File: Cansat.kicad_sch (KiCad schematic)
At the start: 42 parts, among them J1 XT30_BATTERY, J10 Micro_SD_Card, J11 MAX17048_PLACEHOLDER, J2 BMP585_PLACEHOLDER, J3 BNO085_PLACEHOLDER, J4 CC1101_MODULE, J5 BUZZ_CONN, J6 SERVO_OUTPUT, J7 5V_BEC, J8 ESC_4IN1, J9 SGP41_PLACEHOLDER, SW1 SW_SPST, U1 XBee_SMT, U2 ESP32-S3-WROOM-1, U3 INA260, U4 GNSS_MODULE, U5 SHT4x

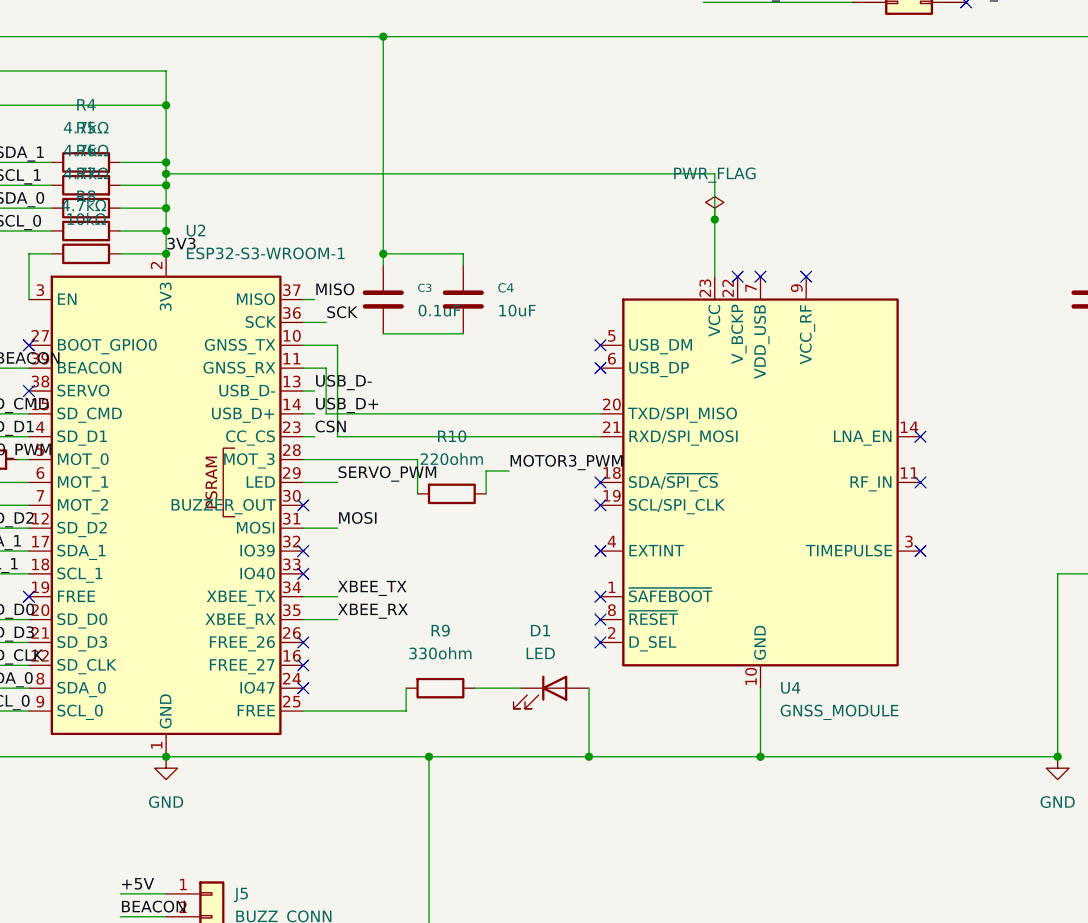
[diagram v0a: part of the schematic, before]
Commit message: replaced GNSS with NavIC 1x06 header
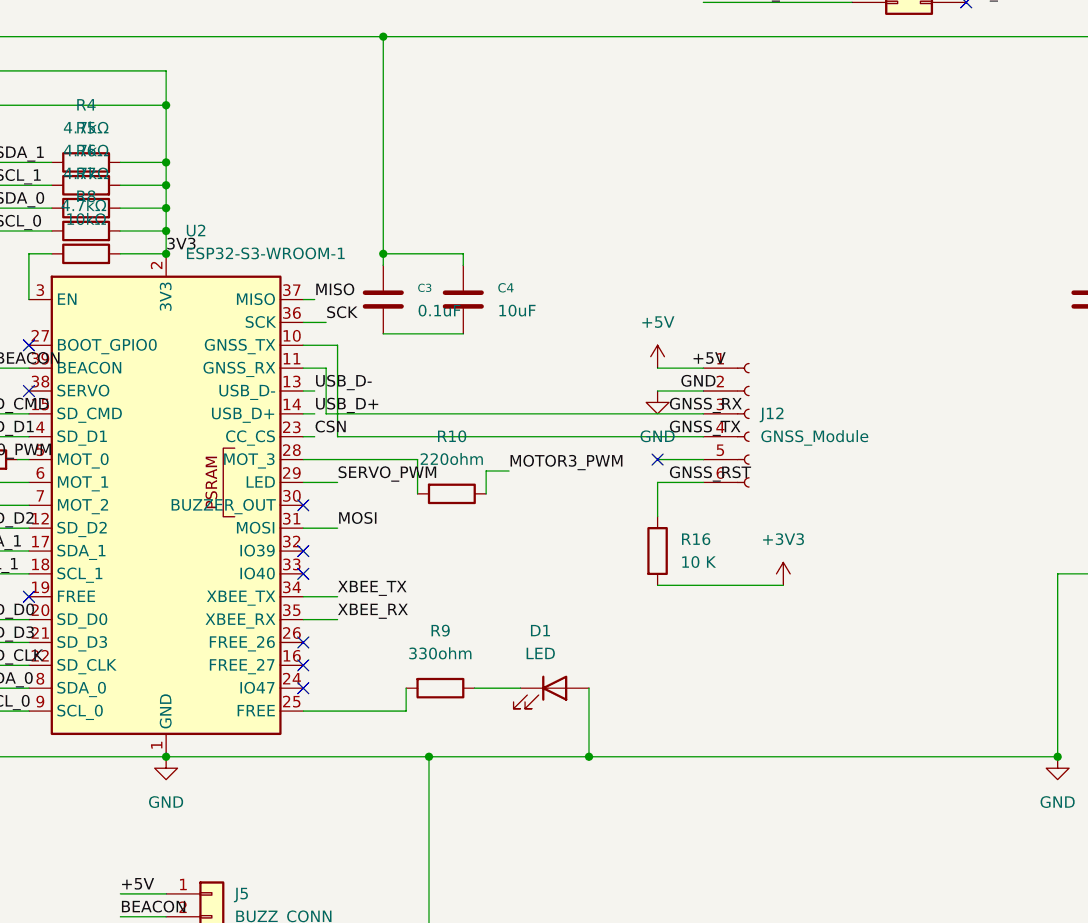
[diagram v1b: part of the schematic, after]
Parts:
- removed U4: GNSS_MODULE, RF_GPS:ublox_NEO, symbol RF_GPS:NEO-M8N
- added J12: GNSS_Module, Connector_PinSocket_2.54mm:PinSocket_1x06_P2.54mm_Vertical, symbol Connector:Conn_01x06_Socket
- added R16: 10 K, symbol Device:R
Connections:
- net +5V: now also J12.1 (Pin_1)
- net GND: now also J12.2 (Pin_2)
- net GNSS_TX: now reaches U2.10 (GNSS_TX)
- net GNSS_TX: now also J12.4 (Pin_4)
- net GNSS_RX: now reaches U2.11 (GNSS_RX)
- net GNSS_RX: now also J12.3 (Pin_3)
- new net +3V3: R16.2
- new net GNSS_RST: J12.6 (Pin_6), R16.1
- no-connect marks 46 -> 33

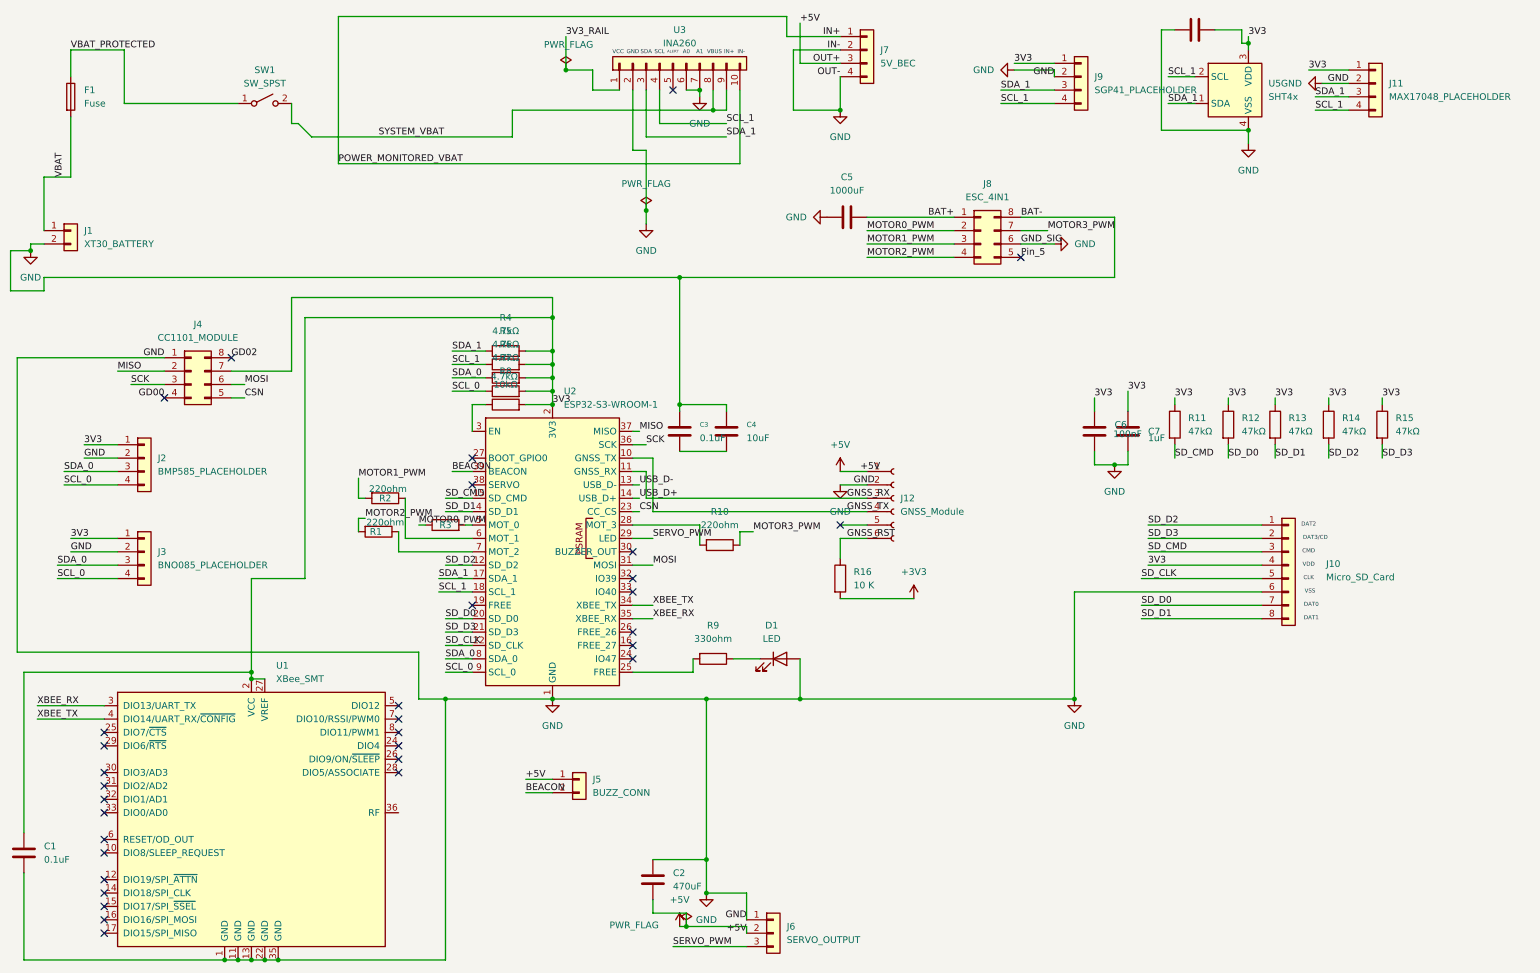
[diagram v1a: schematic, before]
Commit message: Fix V1: Implement proper symbols, SparkFun NEO-F10N, ESP32-S3 breakout, and resolve ERC errors
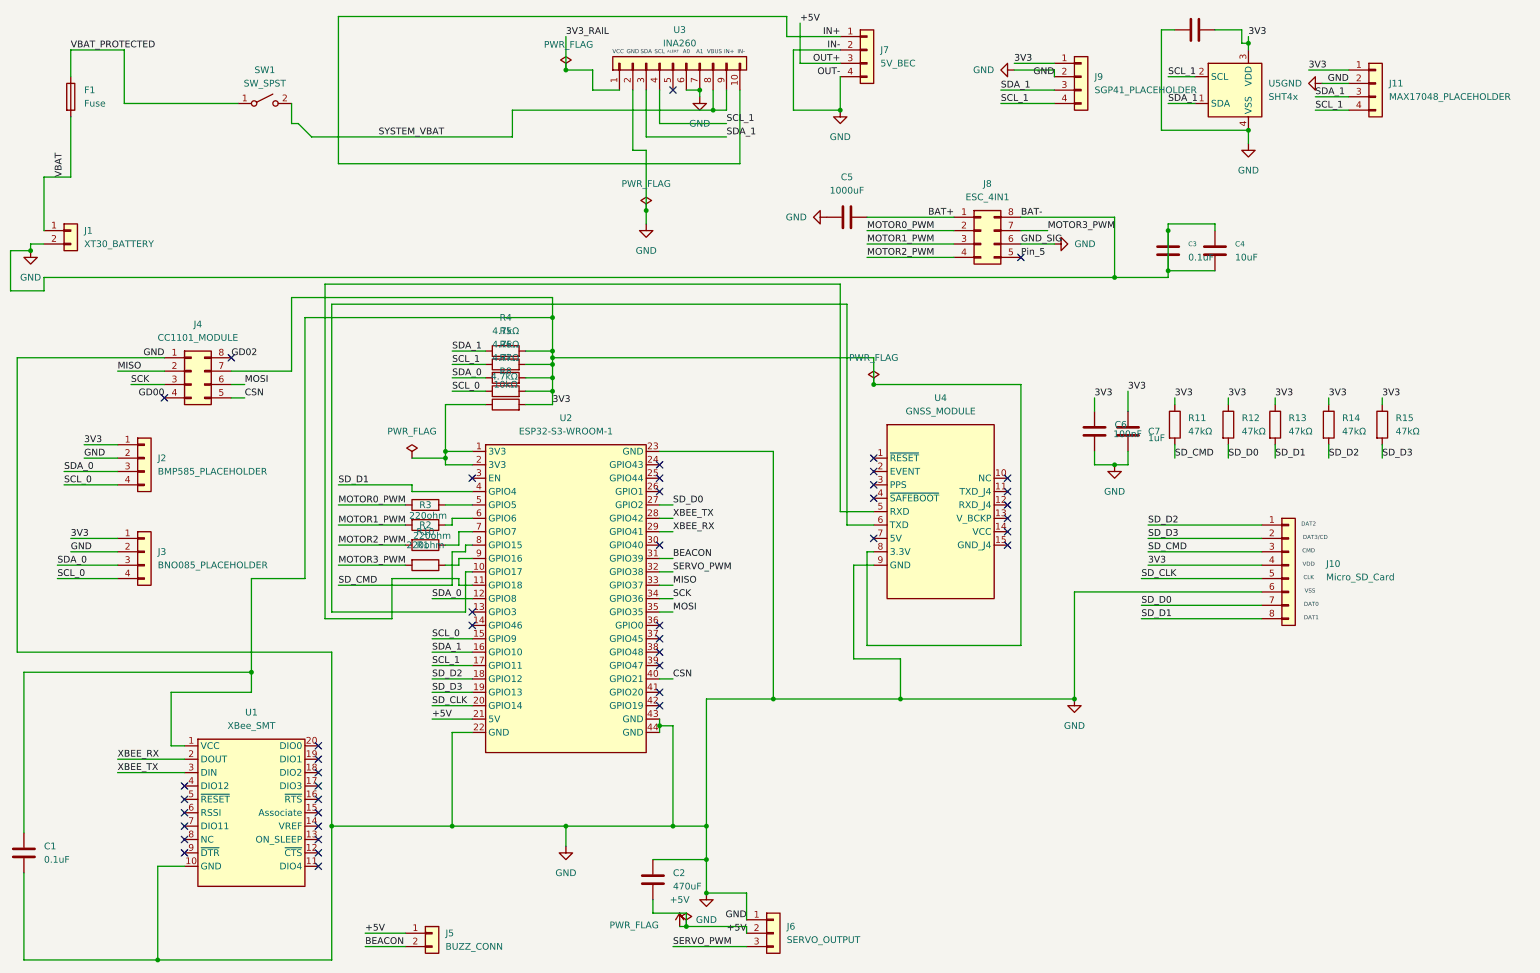
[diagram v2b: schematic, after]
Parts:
- removed D1: LED, LED_THT:LED_D5.0mm, symbol Device:LED
- removed J12: GNSS_Module, Connector_PinSocket_2.54mm:PinSocket_1x06_P2.54mm_Vertical, symbol Connector:Conn_01x06_Socket
- removed R16: 10 K, symbol Device:R
- removed R9: 330ohm, Resistor_THT:R_Axial_DIN0207_L6.3mm_D2.5mm_P2.54mm_Vertical, symbol Device:R
- added U4: GNSS_MODULE, CanSat_Library:NEO_F10N_Breakout, symbol CanSat_Library:NEO_F10N_Breakout
- U1: footprint RF_Module:Digi_XBee_SMT -> CanSat_Library:XBee_3_Pro_TH; symbol RF_ZigBee:XBee_SMT -> CanSat_Library:XBee_3_Pro_TH
- U2: footprint RF_Module:ESP32-S3-WROOM-1 -> PCM_Espressif:ESP32-S3-DevKitC; symbol RF_Module:ESP32-S3-WROOM-1 -> CanSat_Library:ESP32_S3_DevKitC1
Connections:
- net +5V: now also U2.21 (5V)
- net 3V3: now also U1.1 (VCC), U4.8 (3.3V); no longer U1.2 (VCC), U1.27 (VREF), U2.2 (3V3)
- net BEACON: now also U2.31 (GPIO39); no longer U2.39 (BEACON)
- net CSN: now also U2.40 (GPIO21); no longer U2.23 (CC_CS)
- net GND: now also C3.2, C4.2, U1.10 (GND), U2.22 (GND), U2.23 (GND), U2.43 (GND), U2.44 (GND), U4.9 (GND); no longer U1.1 (GND), U1.11 (GND), U1.13 (GND), U1.22 (GND), U1.35 (GND), U2.1 (GND), U2.40 (GND), U2.41 (GND)
- net MISO: now also U2.33 (GPIO37); no longer U2.37 (MISO)
- net MOSI: now also U2.35 (GPIO35); no longer U2.31 (MOSI)
- net MOTOR3_PWM: now also R10.2; no longer R10.1
- net SCK: now also U2.34 (GPIO36); no longer U2.36 (SCK)
- net SCL_0: now also U2.15 (GPIO9); no longer U2.9 (SCL_0)
- net SCL_1: now also U2.17 (GPIO11); no longer U2.18 (SCL_1)
- net SDA_0: now also U2.12 (GPIO8); no longer U2.8 (SDA_0)
- net SDA_1: now also U2.16 (GPIO10); no longer U2.17 (SDA_1)
- net SD_CLK: now also U2.20 (GPIO14); no longer U2.22 (SD_CLK)
- net SD_CMD: now also U2.8 (GPIO15); no longer U2.15 (SD_CMD)
- net SD_D0: now also U2.27 (GPIO2); no longer U2.20 (SD_D0)
- net SD_D2: now also U2.18 (GPIO12); no longer U2.12 (SD_D2)
- net SD_D3: now also U2.19 (GPIO13); no longer U2.21 (SD_D3)
- net SERVO_PWM: now also U2.32 (GPIO38); no longer U2.29 (LED)
- net XBEE_RX: now also U1.2 (DOUT), U2.29 (GPIO41); no longer U1.3 (DIO13/UART_TX), U2.35 (XBEE_RX)
- net XBEE_TX: now also U1.3 (DIN), U2.28 (GPIO42); no longer U1.4 (DIO14/UART_RX/~{CONFIG}), U2.34 (XBEE_TX)
- net at R8.1: now also U2.1 (3V3), U2.2 (3V3); no longer U2.3 (EN)
- net GNSS_RX: no longer names the net of U2.11 (GPIO18)
- net GNSS_RX: now also U4.5 (RXD)
- net GNSS_TX: no longer names the net of U2.10 (GPIO17)
- net GNSS_TX: now also U4.6 (TXD)
- net USB_D+: no longer names the net of U2.14 (GPIO46)
- net USB_D-: no longer names the net of U2.13 (GPIO3)
- new net: R10.1, U2.9 (GPIO16)
- no-connect marks 33 -> 44
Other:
- moved on the sheet: C3, C4, J5, R1, R10, R2, R3

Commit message: Schematic Locked - Zero ERC Errors, Updated Breakouts
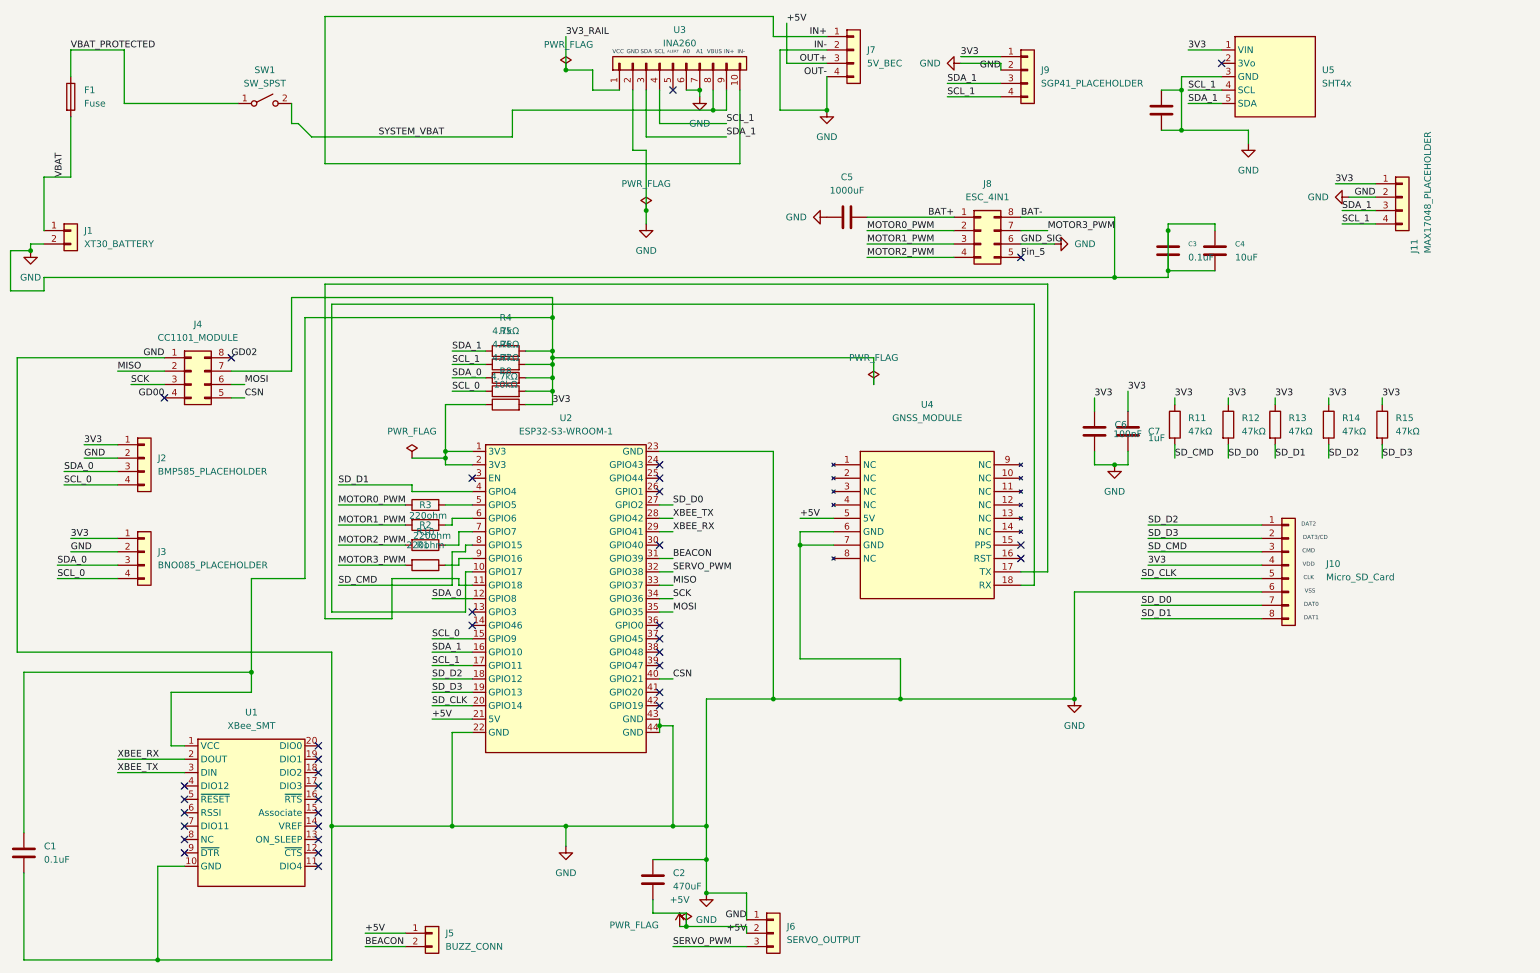
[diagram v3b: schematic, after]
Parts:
- U4: footprint CanSat_Library:NEO_F10N_Breakout -> CanSat_Library:Edgehax_NavIC; symbol CanSat_Library:NEO_F10N_Breakout -> CanSat_Library:Edgehax_NavIC
- U5: footprint Connector_PinSocket_2.54mm:PinSocket_1x04_P2.54mm_Vertical -> Connector_PinSocket_2.54mm:PinSocket_1x05_P2.54mm_Vertical; symbol Sensor_Humidity:SHT4x -> CanSat_Library:SHT4x_Breakout
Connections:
- net +5V: now also U4.5 (5V)
- net 3V3: now also U5.1 (VIN); no longer C8.2, U4.8 (3.3V), U5.3 (VDD)
- net GND: now also C8.2, U4.6 (GND), U4.7 (GND), U5.3 (GND); no longer U4.9 (GND), U5.4 (VSS)
- net SCL_1: now also U5.4 (SCL); no longer U5.2 (SCL)
- net SDA_1: now also U5.5 (SDA); no longer U5.1 (SDA)
- net at U2.10 (GPIO17): now also U4.18 (RX); no longer U4.6 (TXD)
- net at U2.11 (GPIO18): now also U4.17 (TX); no longer U4.5 (RXD)
- no-connect marks 44 -> 36
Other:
- moved on the sheet: J11, J7, J9

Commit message: PDR Bridge Architecture: Generated custom courtyards and board outlines
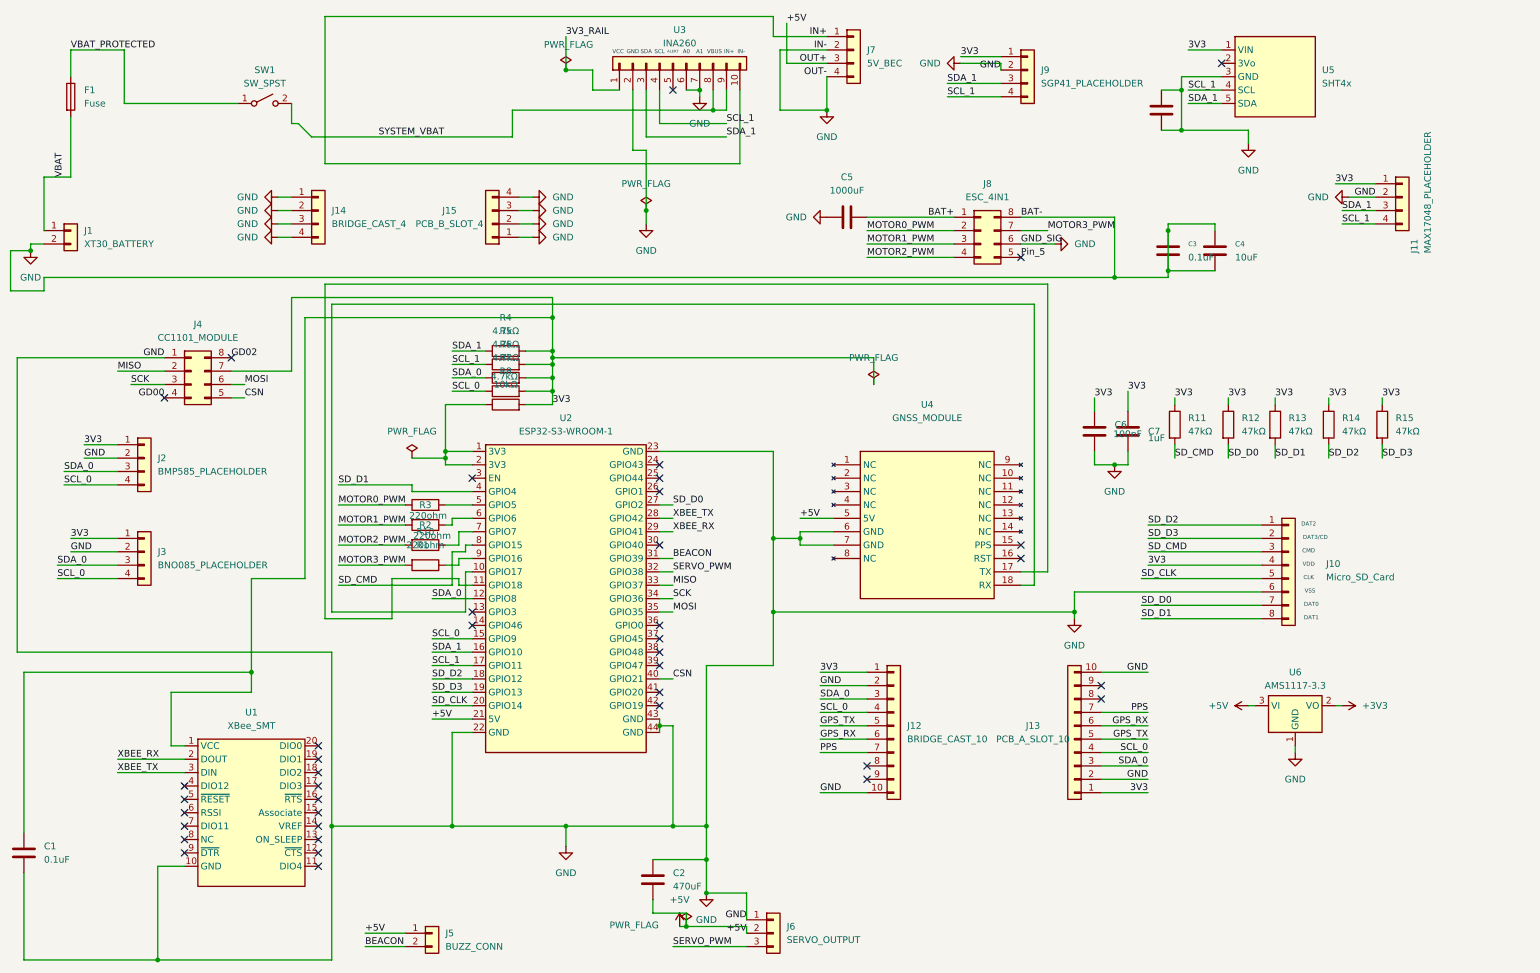
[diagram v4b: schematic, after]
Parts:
- added J12: BRIDGE_CAST_10, CanSat_Library:BRIDGE_CAST_10, symbol Connector_Generic:Conn_01x10
- added J13: PCB_A_SLOT_10, CanSat_Library:MAIN_EDGE_SLOT_10, symbol Connector_Generic:Conn_01x10
- added J14: BRIDGE_CAST_4, CanSat_Library:BRIDGE_CAST_4, symbol Connector_Generic:Conn_01x04
- added J15: PCB_B_SLOT_4, CanSat_Library:MAIN_EDGE_SLOT_4, symbol Connector_Generic:Conn_01x04
- added U6: AMS1117-3.3, Package_TO_SOT_SMD:SOT-223-3_TabPin2, symbol Regulator_Linear:AMS1117-3.3
- J10: footprint Connector_PinSocket_2.54mm:PinSocket_1x08_P2.54mm_Vertical -> CanSat_Library:MicroSD_Breakout
- J11: footprint Connector_PinSocket_2.54mm:PinSocket_1x04_P2.54mm_Vertical -> CanSat_Library:MAX17048_Breakout
- J2: footprint Connector_PinSocket_2.54mm:PinSocket_1x04_P2.54mm_Vertical -> CanSat_Library:BMP585_Breakout
- J3: footprint Connector_PinSocket_2.54mm:PinSocket_1x04_P2.54mm_Vertical -> CanSat_Library:BNO085_Breakout
- J4: footprint Connector_PinSocket_2.54mm:PinSocket_1x08_P2.54mm_Vertical -> CanSat_Library:CC1101_Module
- J7: footprint Connector_PinSocket_2.54mm:PinSocket_1x04_P2.54mm_Vertical -> CanSat_Library:5V_BEC_Pololu
- J8: footprint Connector_PinSocket_2.54mm:PinSocket_1x08_P2.54mm_Vertical -> CanSat_Library:ESC_HAKRC_20A
- J9: footprint Connector_PinSocket_2.54mm:PinSocket_1x04_P2.54mm_Vertical -> CanSat_Library:SGP41_Breakout
- U3: footprint Connector_PinSocket_2.54mm:PinSocket_1x10_P2.54mm_Horizontal -> CanSat_Library:INA260_Breakout
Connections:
- net +5V: now also U6.3 (VI)
- net 3V3: now also J12.1 (Pin_1), J13.1 (Pin_1)
- net GND: now also J12.10 (Pin_10), J12.2 (Pin_2), J13.10 (Pin_10), J13.2 (Pin_2), J14.1 (Pin_1), J14.2 (Pin_2), J14.3 (Pin_3), J14.4 (Pin_4), J15.1 (Pin_1), J15.2 (Pin_2), J15.3 (Pin_3), J15.4 (Pin_4), U6.1 (GND)
- net SCL_0: now also J12.4 (Pin_4), J13.4 (Pin_4)
- net SDA_0: now also J12.3 (Pin_3), J13.3 (Pin_3)
- new net +3V3: U6.2 (VO)
- new net GPS_RX: J12.6 (Pin_6), J13.6 (Pin_6)
- new net GPS_TX: J12.5 (Pin_5), J13.5 (Pin_5)
- new net PPS: J12.7 (Pin_7), J13.7 (Pin_7)
- no-connect marks 36 -> 40
